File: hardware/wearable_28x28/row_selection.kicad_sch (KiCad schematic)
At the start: 99 parts, among them Q201 AO3403, Q202 AO3403, Q203 AO3403, Q204 AO3403, Q205 AO3403, Q206 AO3403, Q207 AO3403, Q208 AO3403, Q209 AO3403, Q210 AO3403, Q211 AO3403, Q212 AO3403, Q213 AO3403, Q214 AO3403, Q215 AO3403, Q216 AO3403, Q217 AO3403, Q218 AO3403, Q219 AO3403, Q220 AO3403, Q221 AO3403, Q222 AO3403, Q223 AO3403, Q224 AO3403, Q225 AO3403, Q226 AO3403, Q227 AO3403, Q228 AO3403, U201 SN74LVC8T245RHLR, U202 74HC154PW,118, U203 74HC154PW,118

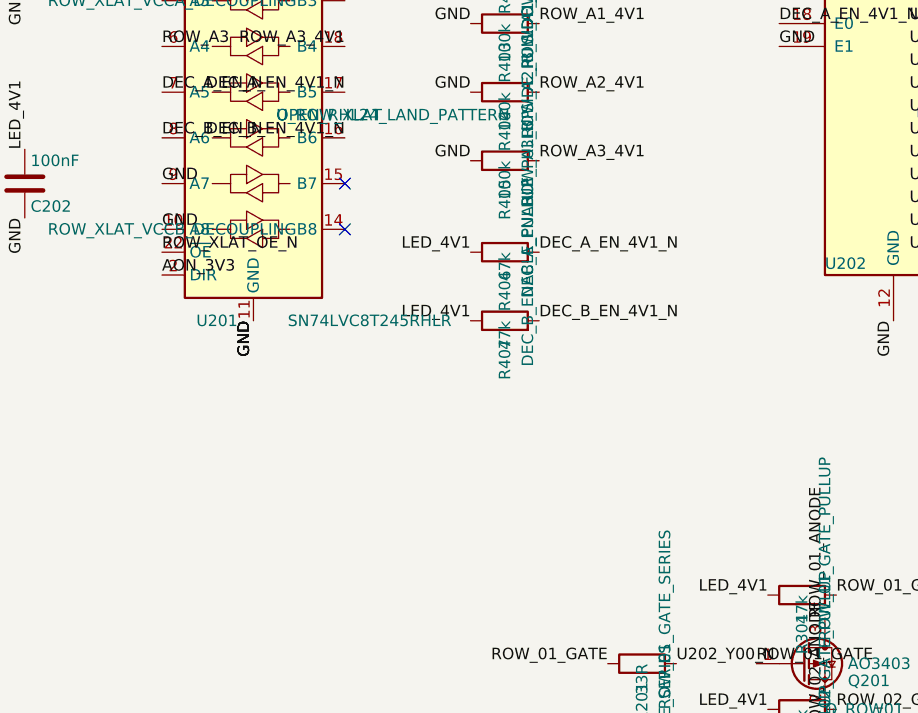
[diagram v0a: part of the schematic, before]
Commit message: Clarify unused translator input grounding
Co-authored-by: illiapliukhin <illiapliukhin@users.noreply.github.com>
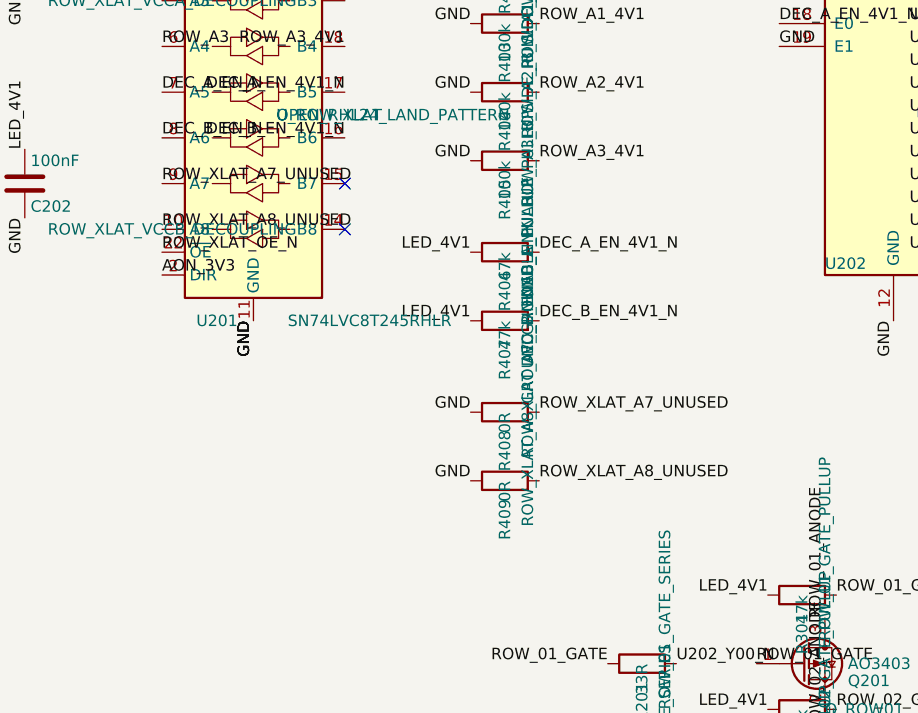
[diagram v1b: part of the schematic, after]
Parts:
- added R408, R409: 0R, Resistor_SMD:R_0603_1608Metric, symbol Device:R
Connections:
- net GND: now also R408.1, R409.1; no longer U201.10 (A8), U201.9 (A7)
- new net ROW_XLAT_A7_UNUSED: R408.2, U201.9 (A7)
- new net ROW_XLAT_A8_UNUSED: R409.2, U201.10 (A8)
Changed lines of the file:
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@@
 		)
 	)
+	(label "ROW_XLAT_A7_UNUSED"
+		(at 45.72 68.58 0)
+		(effects
+			(font
+				(size 1.27 1.27)
+			)
+			(justify left bottom)
+		)
+	)
 	(label "U202_Y04_N"
 		(at 139.7 48.26 180)
@@
 		)
 	)
+	(label "ROW_XLAT_A8_UNUSED"
+		(at 45.72 73.66 0)
+		(effects
+			(font
+				(size 1.27 1.27)
+			)
+			(justify left bottom)
+		)
+	)
 	(label "ROW_07_GATE"
 		(at 120.65 190.5 0)
@@
 		)
 	)
+	(label "ROW_XLAT_A8_UNUSED"
+		(at 87.63 101.6 0)
+		(effects
+			(font
+				(size 1.27 1.27)
+			)
+			(justify left bottom)
+		)
+	)
 	(label "ROW_28_ANODE"
 		(at 314.96 135.89 180)
@@
 		)
 	)
-	(label "GND"
-		(at 45.72 73.66 0)
-		(effects
-			(font
-				(size 1.27 1.27)
-			)
-			(justify left bottom)
-		)
-	)
 	(label "ROW_11_GATE"
 		(at 111.76 248.92 0)
@@
 		)
 	)
-	(label "GND"
-		(at 45.72 68.58 0)
-		(effects
-			(font
-				(size 1.27 1.27)
-			)
-			(justify left bottom)
-		)
-	)
 	(label "LED_4V1"
 		(at 119.38 241.3 270)
@@
 		)
 	)
+	(label "ROW_XLAT_A7_UNUSED"
+		(at 87.63 93.98 0)
+		(effects
+			(font
+				(size 1.27 1.27)
+			)
+			(justify left bottom)
+		)
+	)
 	(label "LED_4V1"
 		(at 220.98 165.1 270)
@@
 		)
 	)
+	(label "GND"
+		(at 80.01 93.98 180)
+		(effects
+			(font
+				(size 1.27 1.27)
+			)
+			(justify right bottom)
+		)
+	)
 	(label "ROW_02_GATE"
 		(at 120.65 127 0)
@@
 	)
 	(label "GND"
+		(at 80.01 101.6 180)
+		(effects
+			(font
+				(size 1.27 1.27)
+			)
+			(justify right bottom)
+		)
+	)
+	(label "GND"
 		(at 80.01 43.18 180)
 		(effects
@@
 	(symbol
 		(lib_id "Device:R")
+		(at 83.82 93.98 90)
+		(unit 1)
+		(body_style 1)
+		(exclude_from_sim no)
+		(in_bom yes)
+		(on_board yes)
+		(in_pos_files yes)
+		(dnp no)
+		(property "Reference" "R408"
+			(at 83.82 96.012 180)
+			(show_name no)
+			(do_not_autoplace no)
+			(effects
+				(font
+					(size 1.27 1.27)
+				)
+				(justify left)
+			)
+		)
+		(property "Value" "0R"
+			(at 83.82 93.98 180)
+			(show_name no)
+			(do_not_autoplace no)
+			(effects
+				(font
+					(size 1.27 1.27)
+				)
+				(justify left)
+			)
+		)
+		(property "Footprint" "Resistor_SMD:R_0603_1608Metric"
+			(at 82.042 93.98 90)
+			(hide yes)
+			(show_name no)
+			(do_not_autoplace no)
+			(effects
+				(font
+					(size 1.27 1.27)
+				)
+			)
+		)
+		(property "Datasheet" ""
+			(at 83.82 93.98 0)
+			(show_name no)
+			(do_not_autoplace no)
+			(effects
+				(font
+					(size 1.27 1.27)
+				)
+			)
+		)
+		(property "Description" ""
+			(at 83.82 93.98 0)
+			(show_name no)
+			(do_not_autoplace no)
+			(effects
+				(font
+					(size 1.27 1.27)
+				)
+			)
+		)
+		(property "Function" "ROW_XLAT_A7_GROUND_LINK"
+			(at 86.36 99.0599 0)
+			(show_name no)
+			(do_not_autoplace no)
+			(effects
+				(font
+					(size 1.27 1.27)
+				)
+				(justify left)
+			)
+		)
+		(pin "1"
+		)
+		(pin "2"
+		)
+		(instances
+			(project "row_selection"
+				(path "/90d886cc-44f6-562e-8bc8-fc6320a84b7f"
+					(reference "R408")
+					(unit 1)
+				)
+			)
+		)
+	)
+	(symbol
+		(lib_id "Device:R")
 		(at 116.84 190.5 90)
 		(unit 1)
@@
 					(unit 1)
 				)
+			)
+		)
+	)
+	(symbol
+		(lib_id "Device:R")
+		(at 83.82 101.6 90)
+		(unit 1)
+		(body_style 1)
+		(exclude_from_sim no)
+		(in_bom yes)
+		(on_board yes)
+		(in_pos_files yes)
+		(dnp no)
+		(property "Reference" "R409"
+			(at 83.82 103.632 180)
+			(show_name no)
+			(do_not_autoplace no)
+			(effects
+				(font
+					(size 1.27 1.27)
+				)
+				(justify left)
+			)
+		)
+		(property "Value" "0R"
+			(at 83.82 101.6 180)
+			(show_name no)
+			(do_not_autoplace no)
+			(effects
+				(font
+					(size 1.27 1.27)
+				)
+				(justify left)
+			)
+		)
+		(property "Footprint" "Resistor_SMD:R_0603_1608Metric"
+			(at 82.042 101.6 90)
+			(hide yes)
+			(show_name no)
+			(do_not_autoplace no)
+			(effects
+				(font
+					(size 1.27 1.27)
+				)
+			)
+		)
+		(property "Datasheet" ""
+			(at 83.82 101.6 0)
+			(show_name no)
+			(do_not_autoplace no)
+			(effects
+				(font
+					(size 1.27 1.27)
+				)
+			)
+		)
+		(property "Description" ""
+			(at 83.82 101.6 0)
+			(show_name no)
+			(do_not_autoplace no)
+			(effects
+				(font
+					(size 1.27 1.27)
+				)
+			)
+		)
+		(property "Function" "ROW_XLAT_A8_GROUND_LINK"
+			(at 86.36 106.6799 0)
+			(show_name no)
+			(do_not_autoplace no)
+			(effects
+				(font
+					(size 1.27 1.27)
+				)
+				(justify left)
+			)
+		)
+		(pin "1"
+		)
+		(pin "2"
+		)
+		(instances
+			(project "row_selection"
+				(path "/90d886cc-44f6-562e-8bc8-fc6320a84b7f"
+					(reference "R409")
+					(unit 1)
+				)

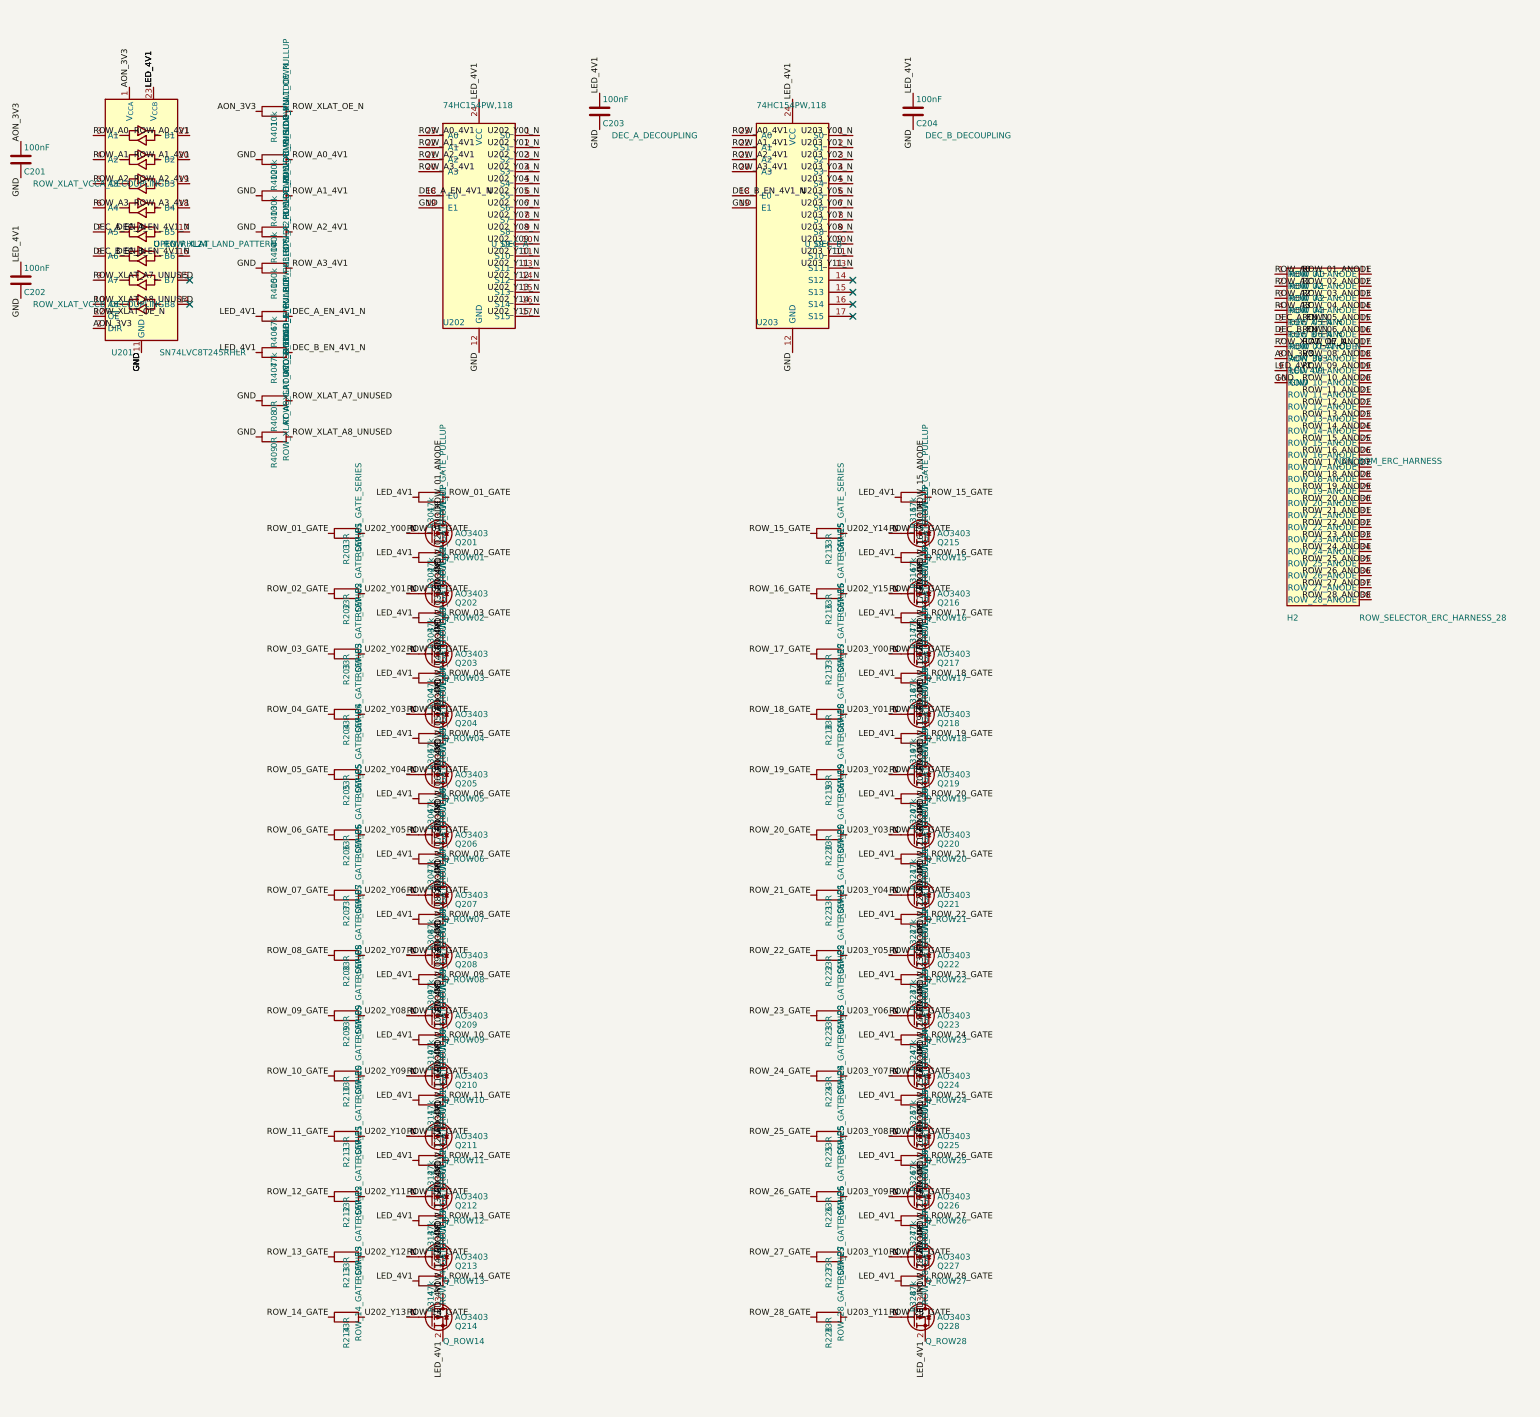
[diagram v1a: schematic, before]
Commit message: Preserve row resistor pin mapping
Co-authored-by: illiapliukhin <illiapliukhin@users.noreply.github.com>
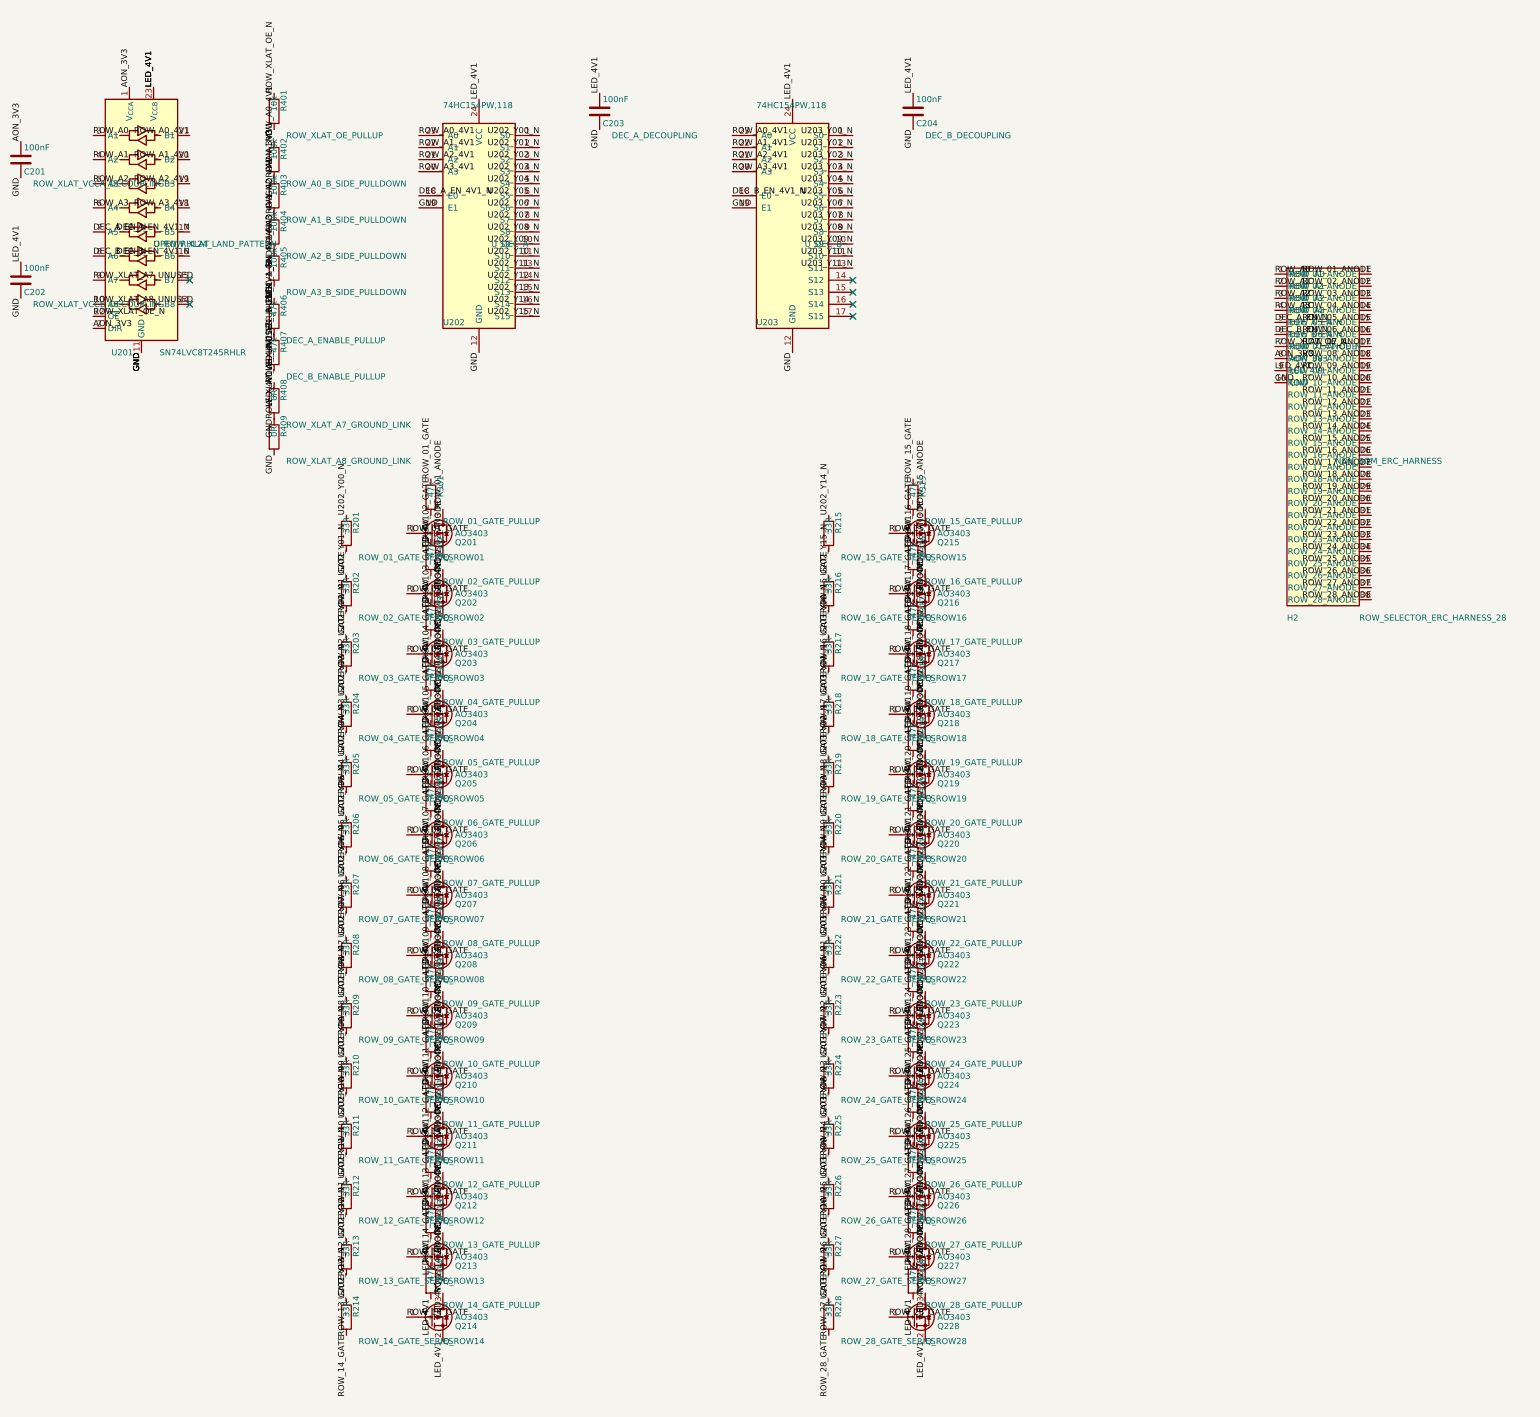
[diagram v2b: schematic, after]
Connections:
- net ROW_A1_4V1 is gone; now on net GND: R403.2, U201.20 (B2), U202.22 (A1), U203.22 (A1)
- net ROW_A2_4V1 is gone; now on net GND: R404.2, U201.19 (B3), U202.21 (A2), U203.21 (A2)
- net ROW_A3_4V1 is gone; now on net GND: R405.2, U201.18 (B4), U202.20 (A3), U203.20 (A3)
- net ROW_XLAT_A8_UNUSED is gone; now on net GND: R409.2, U201.10 (A8)
- net AON_3V3: now also R401.2; no longer R401.1
- net DEC_A_EN_4V1_N: now also R406.1; no longer R406.2
- net DEC_B_EN_4V1_N: now also C202.1, C203.1, C204.1, H2.9 (LED_4V1), Q201.2 (S), Q202.2 (S), Q203.2 (S), Q204.2 (S), Q205.2 (S), Q206.2 (S), Q207.2 (S), Q208.2 (S), Q209.2 (S), Q210.2 (S), Q211.2 (S), Q212.2 (S), Q213.2 (S), Q214.2 (S), Q215.2 (S), Q216.2 (S), Q217.2 (S), Q218.2 (S), Q219.2 (S), Q220.2 (S), Q221.2 (S), Q222.2 (S), Q223.2 (S), Q224.2 (S), Q225.2 (S), Q226.2 (S), Q227.2 (S), Q228.2 (S), R301.2, R302.2, R303.2, R304.2, R305.2, R306.2, R307.2, R308.2, R309.2, R310.2, R311.2, R312.2, R313.2, R314.2, R315.2, R316.2, R317.2, R318.2, R319.2, R320.2, R321.2, R322.2, R323.2, R324.2, R325.2, R326.2, R327.2, R328.2, R406.2, R407.1, U201.23 (V_{CCB}), U201.24 (V_{CCB}), U202.24 (VCC), U203.24 (VCC)
- net GND: now also R402.2, R408.2; no longer R402.1, R408.1
- net ROW_01_GATE: now also R201.2, R301.1; no longer R201.1, R301.2
- net ROW_02_GATE: now also R202.2, R302.1; no longer R202.1, R302.2
- net ROW_03_GATE: now also R203.2, R303.1; no longer R203.1, R303.2
- net ROW_04_GATE: now also R204.2, R304.1; no longer R204.1, R304.2
- net ROW_05_GATE: now also R205.2, R305.1; no longer R205.1, R305.2
- net ROW_06_GATE: now also R206.2, R306.1; no longer R206.1, R306.2
- net ROW_07_GATE: now also R207.2, R307.1; no longer R207.1, R307.2
- net ROW_08_GATE: now also R208.2, R308.1; no longer R208.1, R308.2
- net ROW_09_GATE: now also R209.2, R309.1; no longer R209.1, R309.2
- net ROW_10_GATE: now also R210.2, R310.1; no longer R210.1, R310.2
- net ROW_11_GATE: now also R211.2, R311.1; no longer R211.1, R311.2
- net ROW_12_GATE: now also R212.2, R312.1; no longer R212.1, R312.2
- net ROW_13_GATE: now also R213.2, R313.1; no longer R213.1, R313.2
- net ROW_14_GATE: now also R214.2, R314.1; no longer R214.1, R314.2
- net ROW_15_GATE: now also R215.2, R315.1; no longer R215.1, R315.2
- net ROW_16_GATE: now also R216.2, R316.1; no longer R216.1, R316.2
- net ROW_17_GATE: now also R217.2, R317.1; no longer R217.1, R317.2
- net ROW_18_GATE: now also R218.2, R318.1; no longer R218.1, R318.2
- net ROW_19_GATE: now also R219.2, R319.1; no longer R219.1, R319.2
- net ROW_20_GATE: now also R220.2, R320.1; no longer R220.1, R320.2
- net ROW_21_GATE: now also R221.2, R321.1; no longer R221.1, R321.2
- net ROW_22_GATE: now also R222.2, R322.1; no longer R222.1, R322.2
- net ROW_23_GATE: now also R223.2, R323.1; no longer R223.1, R323.2
- net ROW_24_GATE: now also R224.2, R324.1; no longer R224.1, R324.2
- net ROW_25_GATE: now also R225.2, R325.1; no longer R225.1, R325.2
- net ROW_26_GATE: now also R226.2, R326.1; no longer R226.1, R326.2
- net ROW_27_GATE: now also R227.2, R327.1; no longer R227.1, R327.2
- net ROW_28_GATE: now also R228.2, R328.1; no longer R228.1, R328.2
- net ROW_A0_4V1: now also R402.1; no longer R402.2
- net ROW_XLAT_A7_UNUSED: now also R408.1; no longer R408.2
- net ROW_XLAT_OE_N: now also R401.1; no longer R401.2
- net U202_Y00_N: now also R201.1; no longer R201.2
- net U202_Y01_N: now also R202.1; no longer R202.2
- net U202_Y02_N: now also R203.1; no longer R203.2
- net U202_Y03_N: now also R204.1; no longer R204.2
- net U202_Y04_N: now also R205.1; no longer R205.2
- net U202_Y05_N: now also R206.1; no longer R206.2
- net U202_Y06_N: now also R207.1; no longer R207.2
- net U202_Y07_N: now also R208.1; no longer R208.2
- net U202_Y08_N: now also R209.1; no longer R209.2
- net U202_Y09_N: now also R210.1; no longer R210.2
- net U202_Y10_N: now also R211.1; no longer R211.2
- net U202_Y11_N: now also R212.1; no longer R212.2
- net U202_Y12_N: now also R213.1; no longer R213.2
- net U202_Y13_N: now also R214.1; no longer R214.2
- net U202_Y14_N: now also R215.1; no longer R215.2
- net U202_Y15_N: now also R216.1; no longer R216.2
- net U203_Y00_N: now also R217.1; no longer R217.2
- net U203_Y01_N: now also R218.1; no longer R218.2
- net U203_Y02_N: now also R219.1; no longer R219.2
- net U203_Y03_N: now also R220.1; no longer R220.2
- net U203_Y04_N: now also R221.1; no longer R221.2
- net U203_Y05_N: now also R222.1; no longer R222.2
- net U203_Y06_N: now also R223.1; no longer R223.2
- net U203_Y07_N: now also R224.1; no longer R224.2
- net U203_Y08_N: now also R225.1; no longer R225.2
- net U203_Y09_N: now also R226.1; no longer R226.2
- net U203_Y10_N: now also R227.1; no longer R227.2
- net U203_Y11_N: now also R228.1; no longer R228.2
- removed net LED_4V1: C202.1, C203.1, C204.1, H2.9 (LED_4V1), Q201.2 (S), Q202.2 (S), Q203.2 (S), Q204.2 (S), Q205.2 (S), Q206.2 (S), Q207.2 (S), Q208.2 (S), Q209.2 (S), Q210.2 (S), Q211.2 (S), Q212.2 (S), Q213.2 (S), Q214.2 (S), Q215.2 (S), Q216.2 (S), Q217.2 (S), Q218.2 (S), Q219.2 (S), Q220.2 (S), Q221.2 (S), Q222.2 (S), Q223.2 (S), Q224.2 (S), Q225.2 (S), Q226.2 (S), Q227.2 (S), Q228.2 (S), R301.1, R302.1, R303.1, R304.1, R305.1, R306.1, R307.1, R308.1, R309.1, R310.1, R311.1, R312.1, R313.1, R314.1, R315.1, R316.1, R317.1, R318.1, R319.1, R320.1, R321.1, R322.1, R323.1, R324.1, R325.1, R326.1, R327.1, R328.1, R406.1, R407.1, U201.23 (V_{CCB}), U201.24 (V_{CCB}), U202.24 (VCC), U203.24 (VCC)
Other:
- moved on the sheet: R201, R202, R203, R204, R205, R206, R207, R208, R209, R210, R211, R212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

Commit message: Separate row resistor label endpoints
Co-authored-by: illiapliukhin <illiapliukhin@users.noreply.github.com>
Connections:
- net DEC_B_EN_4V1_N: no longer C202.1, C203.1, C204.1, H2.9 (LED_4V1), Q201.2 (S), Q202.2 (S), Q203.2 (S), Q204.2 (S), Q205.2 (S), Q206.2 (S), Q207.2 (S), Q208.2 (S), Q209.2 (S), Q210.2 (S), Q211.2 (S), Q212.2 (S), Q213.2 (S), Q214.2 (S), Q215.2 (S), Q216.2 (S), Q217.2 (S), Q218.2 (S), Q219.2 (S), Q220.2 (S), Q221.2 (S), Q222.2 (S), Q223.2 (S), Q224.2 (S), Q225.2 (S), Q226.2 (S), Q227.2 (S), Q228.2 (S), R301.2, R302.2, R303.2, R304.2, R305.2, R306.2, R307.2, R308.2, R309.2, R310.2, R311.2, R312.2, R313.2, R314.2, R315.2, R316.2, R317.2, R318.2, R319.2, R320.2, R321.2, R322.2, R323.2, R324.2, R325.2, R326.2, R327.2, R328.2, R406.2, R407.2, U201.23 (V_{CCB}), U201.24 (V_{CCB}), U202.24 (VCC), U203.24 (VCC)
- net GND: no longer R403.1, R404.1, R405.1, R409.1, U201.10 (A8), U201.18 (B4), U201.19 (B3), U201.20 (B2), U202.20 (A3), U202.21 (A2), U202.22 (A1), U203.20 (A3), U203.21 (A2), U203.22 (A1)
- new net LED_4V1: C202.1, C203.1, C204.1, H2.9 (LED_4V1), Q201.2 (S), Q202.2 (S), Q203.2 (S), Q204.2 (S), Q205.2 (S), Q206.2 (S), Q207.2 (S), Q208.2 (S), Q209.2 (S), Q210.2 (S), Q211.2 (S), Q212.2 (S), Q213.2 (S), Q214.2 (S), Q215.2 (S), Q216.2 (S), Q217.2 (S), Q218.2 (S), Q219.2 (S), Q220.2 (S), Q221.2 (S), Q222.2 (S), Q223.2 (S), Q224.2 (S), Q225.2 (S), Q226.2 (S), Q227.2 (S), Q228.2 (S), R301.2, R302.2, R303.2, R304.2, R305.2, R306.2, R307.2, R308.2, R309.2, R310.2, R311.2, R312.2, R313.2, R314.2, R315.2, R316.2, R317.2, R318.2, R319.2, R320.2, R321.2, R322.2, R323.2, R324.2, R325.2, R326.2, R327.2, R328.2, R406.2, R407.2, U201.23 (V_{CCB}), U201.24 (V_{CCB}), U202.24 (VCC), U203.24 (VCC)
- new net ROW_A1_4V1: R403.1, U201.20 (B2), U202.22 (A1), U203.22 (A1)
- new net ROW_A2_4V1: R404.1, U201.19 (B3), U202.21 (A2), U203.21 (A2)
- new net ROW_A3_4V1: R405.1, U201.18 (B4), U202.20 (A3), U203.20 (A3)
- new net ROW_XLAT_A8_UNUSED: R409.1, U201.10 (A8)
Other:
- moved on the sheet: R201, R202, R203, R204, R205, R206, R207, R208, R209, R210, R211, R212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
